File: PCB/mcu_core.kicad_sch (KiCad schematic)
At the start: 10 parts

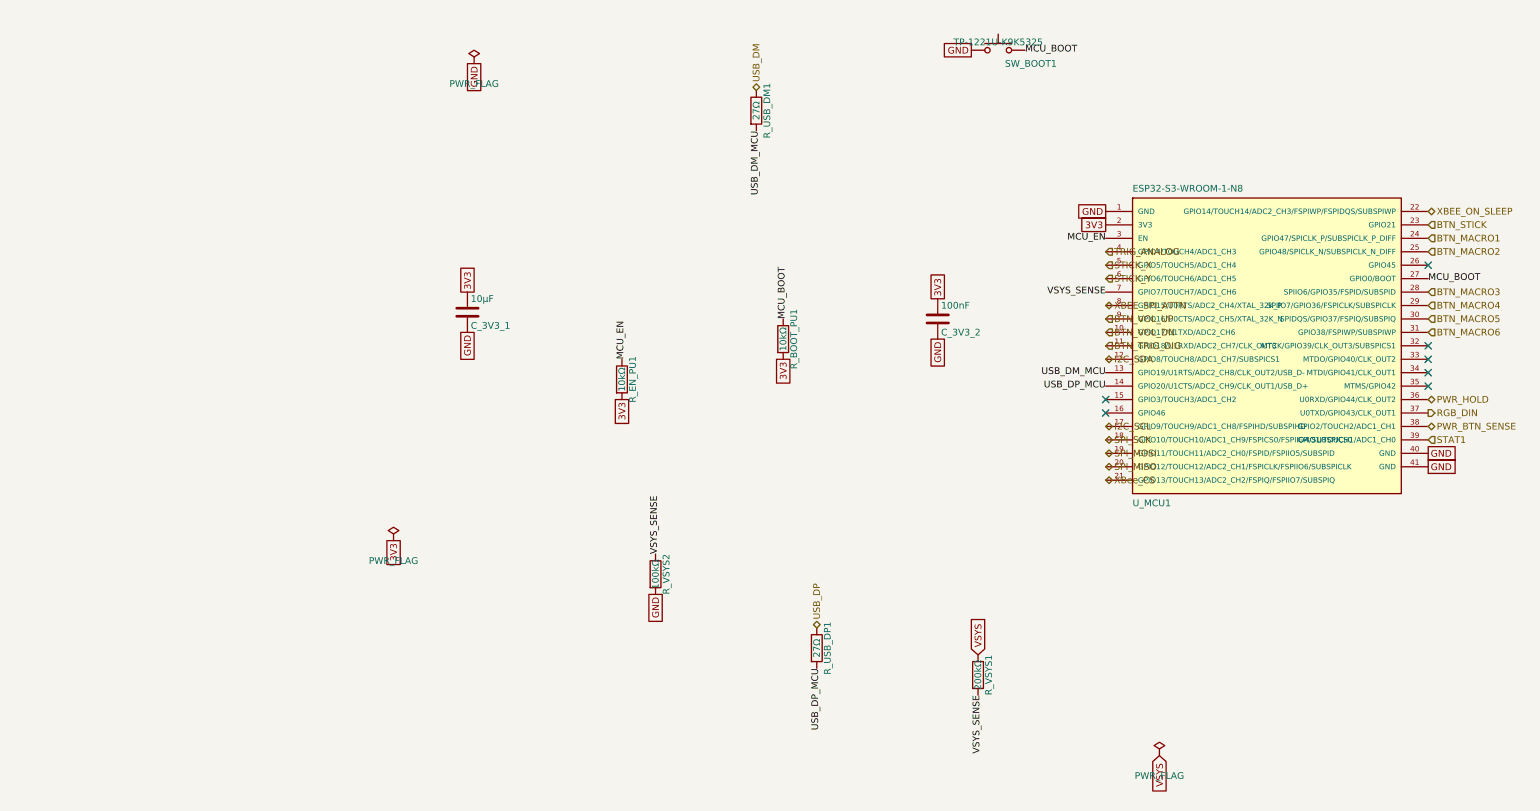
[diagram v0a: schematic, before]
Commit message: refactor: updated gulikit footprint
This updates the gulikit thumbstick footprint to be accurate.
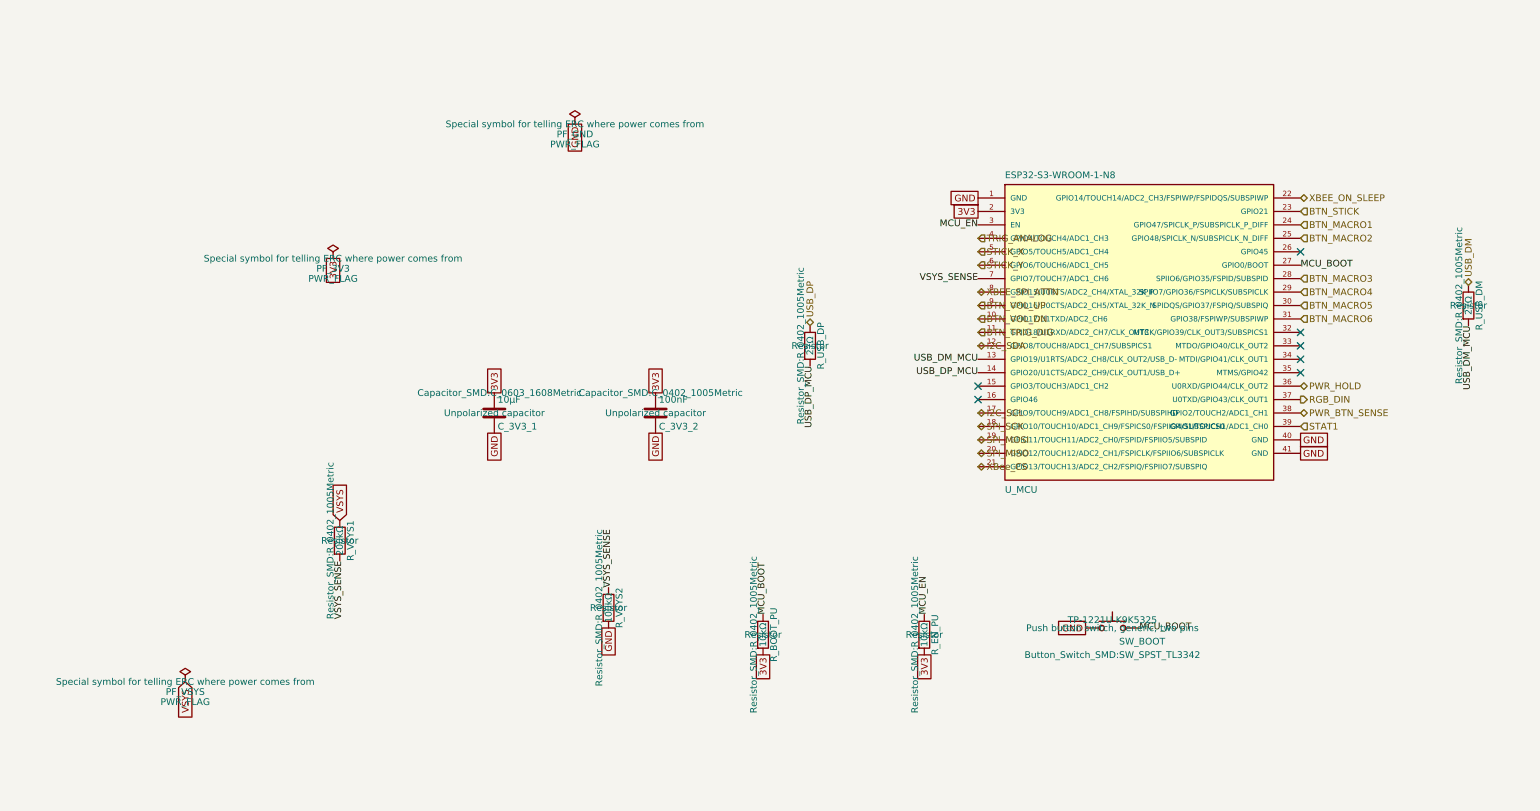
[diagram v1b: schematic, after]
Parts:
- removed R_BOOT_PU1, R_EN_PU1: 10kΩ, Resistor_SMD:R_0402_1005Metric, symbol Device:R
- removed R_USB_DM1, R_USB_DP1: 27Ω, Resistor_SMD:R_0402_1005Metric, symbol Device:R
- removed SW_BOOT1: TP-1221U-K9K5325, Button_Switch_SMD:SW_SPST_TL3342, symbol Switch:SW_Push
- removed U_MCU1: ESP32-S3-WROOM-1-N8, Espressif:ESP32-S3-WROOM-1, symbol Espressif:ESP32-S3-WROOM-1
- added PF_3V3, PF_GND, PF_VSYS: PWR_FLAG, symbol power:PWR_FLAG
- added R_BOOT_PU, R_EN_PU: 10kΩ, Resistor_SMD:R_0402_1005Metric, symbol Device:R
- added R_USB_DM, R_USB_DP: 27Ω, Resistor_SMD:R_0402_1005Metric, symbol Device:R
- added SW_BOOT: TP-1221U-K9K5325, Button_Switch_SMD:SW_SPST_TL3342, symbol Switch:SW_Push
- added U_MCU: ESP32-S3-WROOM-1-N8, Espressif:ESP32-S3-WROOM-1, symbol Espressif:ESP32-S3-WROOM-1
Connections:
- net 3V3: now also PF_3V3.1, R_BOOT_PU.2, R_EN_PU.2, U_MCU.2 (3V3)
- net BTN_MACRO1: now also U_MCU.24 (GPIO47/SPICLK_P/SUBSPICLK_P_DIFF)
- net BTN_MACRO2: now also U_MCU.25 (GPIO48/SPICLK_N/SUBSPICLK_N_DIFF)
- net BTN_MACRO3: now also U_MCU.28 (SPIIO6/GPIO35/FSPID/SUBSPID)
- net BTN_MACRO4: now also U_MCU.29 (SPIIO7/GPIO36/FSPICLK/SUBSPICLK)
- net BTN_MACRO5: now also U_MCU.30 (SPIDQS/GPIO37/FSPIQ/SUBSPIQ)
- net BTN_MACRO6: now also U_MCU.31 (GPIO38/FSPIWP/SUBSPIWP)
- net BTN_STICK: now also U_MCU.23 (GPIO21)
- net BTN_TRIG_DIG: now also U_MCU.11 (GPIO18/U1RXD/ADC2_CH7/CLK_OUT3)
- net BTN_VOL_DN: now also U_MCU.10 (GPIO17/U1TXD/ADC2_CH6)
- net BTN_VOL_UP: now also U_MCU.9 (GPIO16/U0CTS/ADC2_CH5/XTAL_32K_N)
- net GND: now also PF_GND.1, SW_BOOT.1, U_MCU.1 (GND), U_MCU.40 (GND), U_MCU.41 (GND)
- net I2C_SCL: now also U_MCU.17 (GPIO9/TOUCH9/ADC1_CH8/FSPIHD/SUBSPIHD)
- net I2C_SDA: now also U_MCU.12 (GPIO8/TOUCH8/ADC1_CH7/SUBSPICS1)
- net MCU_BOOT: now also R_BOOT_PU.1, SW_BOOT.2, U_MCU.27 (GPIO0/BOOT)
- net MCU_EN: now also R_EN_PU.1, U_MCU.3 (EN)
- net PWR_BTN_SENSE: now also U_MCU.38 (GPIO2/TOUCH2/ADC1_CH1)
- net PWR_HOLD: now also U_MCU.36 (U0RXD/GPIO44/CLK_OUT2)
- net RGB_DIN: now also U_MCU.37 (U0TXD/GPIO43/CLK_OUT1)
- net SPI_MISO: now also U_MCU.20 (GPIO12/TOUCH12/ADC2_CH1/FSPICLK/FSPIIO6/SUBSPICLK)
- net SPI_MOSI: now also U_MCU.19 (GPIO11/TOUCH11/ADC2_CH0/FSPID/FSPIIO5/SUBSPID)
- net SPI_SCK: now also U_MCU.18 (GPIO10/TOUCH10/ADC1_CH9/FSPICS0/FSPIIO4/SUBSPICS0)
- net STAT1: now also U_MCU.39 (GPIO1/TOUCH1/ADC1_CH0)
- net STICK_X: now also U_MCU.5 (GPIO5/TOUCH5/ADC1_CH4)
- net STICK_Y: now also U_MCU.6 (GPIO6/TOUCH6/ADC1_CH5)
- net TRIG_ANALOG: now also U_MCU.4 (GPIO4/TOUCH4/ADC1_CH3)
- net USB_DM: now also R_USB_DM.1
- net USB_DM_MCU: now also R_USB_DM.2, U_MCU.13 (GPIO19/U1RTS/ADC2_CH8/CLK_OUT2/USB_D-)
- net USB_DP: now also R_USB_DP.1
- net USB_DP_MCU: now also R_USB_DP.2, U_MCU.14 (GPIO20/U1CTS/ADC2_CH9/CLK_OUT1/USB_D+)
- net VSYS: now also PF_VSYS.1
- net VSYS_SENSE: now also U_MCU.7 (GPIO7/TOUCH7/ADC1_CH6)
- net XBEE_ON_SLEEP: now also U_MCU.22 (GPIO14/TOUCH14/ADC2_CH3/FSPIWP/FSPIDQS/SUBSPIWP)
- net XBEE_SPI_ATTN: now also U_MCU.8 (GPIO15/U0RTS/ADC2_CH4/XTAL_32K_P)
- net XBee_CS: now also U_MCU.21 (GPIO13/TOUCH13/ADC2_CH2/FSPIQ/FSPIIO7/SUBSPIQ)

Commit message: layout: beginning pcb layout
This updates the schematic with a few different footprints while also starts the layout.
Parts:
- removed PF_3V3, PF_GND, PF_VSYS: PWR_FLAG, symbol power:PWR_FLAG
- renumbered R_BOOT_PU to R_BOOT_PU1, R_EN_PU to R_EN_PU1, R_USB_DM to R_USB_DM1, R_USB_DP to R_USB_DP1, SW_BOOT to SW_BOOT1, U_MCU to U_MCU1
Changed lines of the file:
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@@
 		(dnp no)
 		(fields_autoplaced yes)
-		(property "Reference" "PF_GND"
+		(property "Reference" "PF_GND01"
 			(at 100.33 53.975 0)
 			(show_name no)
@@
 		)
 		(instances
+			(project "snips_controller"
+				(path "/868f8289-8434-4465-b2f4-2accc5e40bab/c3894f85-0389-4f3d-bfa3-88715bea0c3d"
+					(reference "PF_GND01")
+					(unit 1)
+				)
+			)
 			(project ""
 				(path "/d0f5b7d7-b2b6-4492-958c-e60265d3c6b4/c3894f85-0389-4f3d-bfa3-88715bea0c3d"
@@
 		(dnp no)
 		(fields_autoplaced yes)
-		(property "Reference" "U_MCU"
+		(property "Reference" "U_MCU1"
 			(at 181.61 121.92 0)
 			(show_name no)
@@
 		)
 		(instances
+			(project "snips_controller"
+				(path "/868f8289-8434-4465-b2f4-2accc5e40bab/c3894f85-0389-4f3d-bfa3-88715bea0c3d"
+					(reference "U_MCU1")
+					(unit 1)
+				)
+			)
 			(project ""
 				(path "/d0f5b7d7-b2b6-4492-958c-e60265d3c6b4/c3894f85-0389-4f3d-bfa3-88715bea0c3d"
@@
 		(dnp no)
 		(fields_autoplaced yes)
-		(property "Reference" "R_USB_DM"
+		(property "Reference" "R_USB_DM1"
 			(at 271.272 86.36 90)
 			(show_name no)
@@
 		)
 		(instances
+			(project "snips_controller"
+				(path "/868f8289-8434-4465-b2f4-2accc5e40bab/c3894f85-0389-4f3d-bfa3-88715bea0c3d"
+					(reference "R_USB_DM1")
+					(unit 1)
+				)
+			)
 			(project ""
 				(path "/d0f5b7d7-b2b6-4492-958c-e60265d3c6b4/c3894f85-0389-4f3d-bfa3-88715bea0c3d"
@@
 		(dnp no)
 		(fields_autoplaced yes)
-		(property "Reference" "R_EN_PU"
+		(property "Reference" "R_EN_PU1"
 			(at 168.402 148.59 90)
 			(show_name no)
@@
 		)
 		(instances
+			(project "snips_controller"
+				(path "/868f8289-8434-4465-b2f4-2accc5e40bab/c3894f85-0389-4f3d-bfa3-88715bea0c3d"
+					(reference "R_EN_PU1")
+					(unit 1)
+				)
+			)
 			(project ""
 				(path "/d0f5b7d7-b2b6-4492-958c-e60265d3c6b4/c3894f85-0389-4f3d-bfa3-88715bea0c3d"
@@
 		(dnp no)
 		(fields_autoplaced yes)
-		(property "Reference" "PF_VSYS"
+		(property "Reference" "PF_VSYS01"
 			(at 26.67 159.385 0)
 			(show_name no)
@@
 		)
 		(instances
+			(project "snips_controller"
+				(path "/868f8289-8434-4465-b2f4-2accc5e40bab/c3894f85-0389-4f3d-bfa3-88715bea0c3d"
+					(reference "PF_VSYS01")
+					(unit 1)
+				)
+			)
 			(project ""
 				(path "/d0f5b7d7-b2b6-4492-958c-e60265d3c6b4/c3894f85-0389-4f3d-bfa3-88715bea0c3d"
@@
 		(dnp no)
 		(fields_autoplaced yes)
-		(property "Reference" "R_BOOT_PU"
+		(property "Reference" "R_BOOT_PU1"
 			(at 137.922 148.59 90)
 			(show_name no)
@@
 		)
 		(instances
+			(project "snips_controller"
+				(path "/868f8289-8434-4465-b2f4-2accc5e40bab/c3894f85-0389-4f3d-bfa3-88715bea0c3d"
+					(reference "R_BOOT_PU1")
+					(unit 1)
+				)
+			)
 			(project ""
 				(path "/d0f5b7d7-b2b6-4492-958c-e60265d3c6b4/c3894f85-0389-4f3d-bfa3-88715bea0c3d"
@@
 		)
 		(instances
+			(project "snips_controller"
+				(path "/868f8289-8434-4465-b2f4-2accc5e40bab/c3894f85-0389-4f3d-bfa3-88715bea0c3d"
+					(reference "PF_3V3")
+					(unit 1)
+				)
+			)
 			(project ""
 				(path "/d0f5b7d7-b2b6-4492-958c-e60265d3c6b4/c3894f85-0389-4f3d-bfa3-88715bea0c3d"
@@
 		)
 		(instances
+			(project "snips_controller"
+				(path "/868f8289-8434-4465-b2f4-2accc5e40bab/c3894f85-0389-4f3d-bfa3-88715bea0c3d"
+					(reference "R_VSYS1")
+					(unit 1)
+				)
+			)
 			(project ""
 				(path "/d0f5b7d7-b2b6-4492-958c-e60265d3c6b4/c3894f85-0389-4f3d-bfa3-88715bea0c3d"
@@
 		)
 		(instances
+			(project "snips_controller"
+				(path "/868f8289-8434-4465-b2f4-2accc5e40bab/c3894f85-0389-4f3d-bfa3-88715bea0c3d"
+					(reference "C_3V3_2")
+					(unit 1)
+				)
+			)
 			(project ""
 				(path "/d0f5b7d7-b2b6-4492-958c-e60265d3c6b4/c3894f85-0389-4f3d-bfa3-88715bea0c3d"
@@
 		(dnp no)
 		(fields_autoplaced yes)
-		(property "Reference" "SW_BOOT"
+		(property "Reference" "SW_BOOT1"
 			(at 203.2 149.86 0)
 			(show_name no)
@@
 		)
 		(instances
+			(project "snips_controller"
+				(path "/868f8289-8434-4465-b2f4-2accc5e40bab/c3894f85-0389-4f3d-bfa3-88715bea0c3d"
+					(reference "SW_BOOT1")
+					(unit 1)
+				)
+			)
 			(project ""
 				(path "/d0f5b7d7-b2b6-4492-958c-e60265d3c6b4/c3894f85-0389-4f3d-bfa3-88715bea0c3d"
@@
 		)
 		(instances
+			(project "snips_controller"
+				(path "/868f8289-8434-4465-b2f4-2accc5e40bab/c3894f85-0389-4f3d-bfa3-88715bea0c3d"
+					(reference "C_3V3_1")
+					(unit 1)
+				)
+			)
 			(project ""
 				(path "/d0f5b7d7-b2b6-4492-958c-e60265d3c6b4/c3894f85-0389-4f3d-bfa3-88715bea0c3d"
@@
 		)
 		(instances
+			(project "snips_controller"
+				(path "/868f8289-8434-4465-b2f4-2accc5e40bab/c3894f85-0389-4f3d-bfa3-88715bea0c3d"
+					(reference "R_VSYS2")
+					(unit 1)
+				)
+			)
 			(project ""
 				(path "/d0f5b7d7-b2b6-4492-958c-e60265d3c6b4/c3894f85-0389-4f3d-bfa3-88715bea0c3d"
@@
 		(dnp no)
 		(fields_autoplaced yes)
-		(property "Reference" "R_USB_DP"
+		(property "Reference" "R_USB_DP1"
 			(at 146.812 93.98 90)
 			(show_name no)
@@
 		)
 		(instances
-			(project ""
-				(path "/d0f5b7d7-b2b6-4492-958c-e60265d3c6b4/c3894f85-0389-4f3d-bfa3-88715bea0c3d"
+			(project "snips_controller"
+				(path "/868f8289-8434-4465-b2f4-2accc5e40bab/c3894f85-0389-4f3d-bfa3-88715bea0c3d"
+					(reference "R_USB_DP1")
+					(unit 1)
+				)
+			)
+			(project ""
+				(path "/d0f5b7d7-b2b6-4492-958c-e60265d3c6b4/c3894f85-0389-4f3d-bfa3-88715bea0c3d"

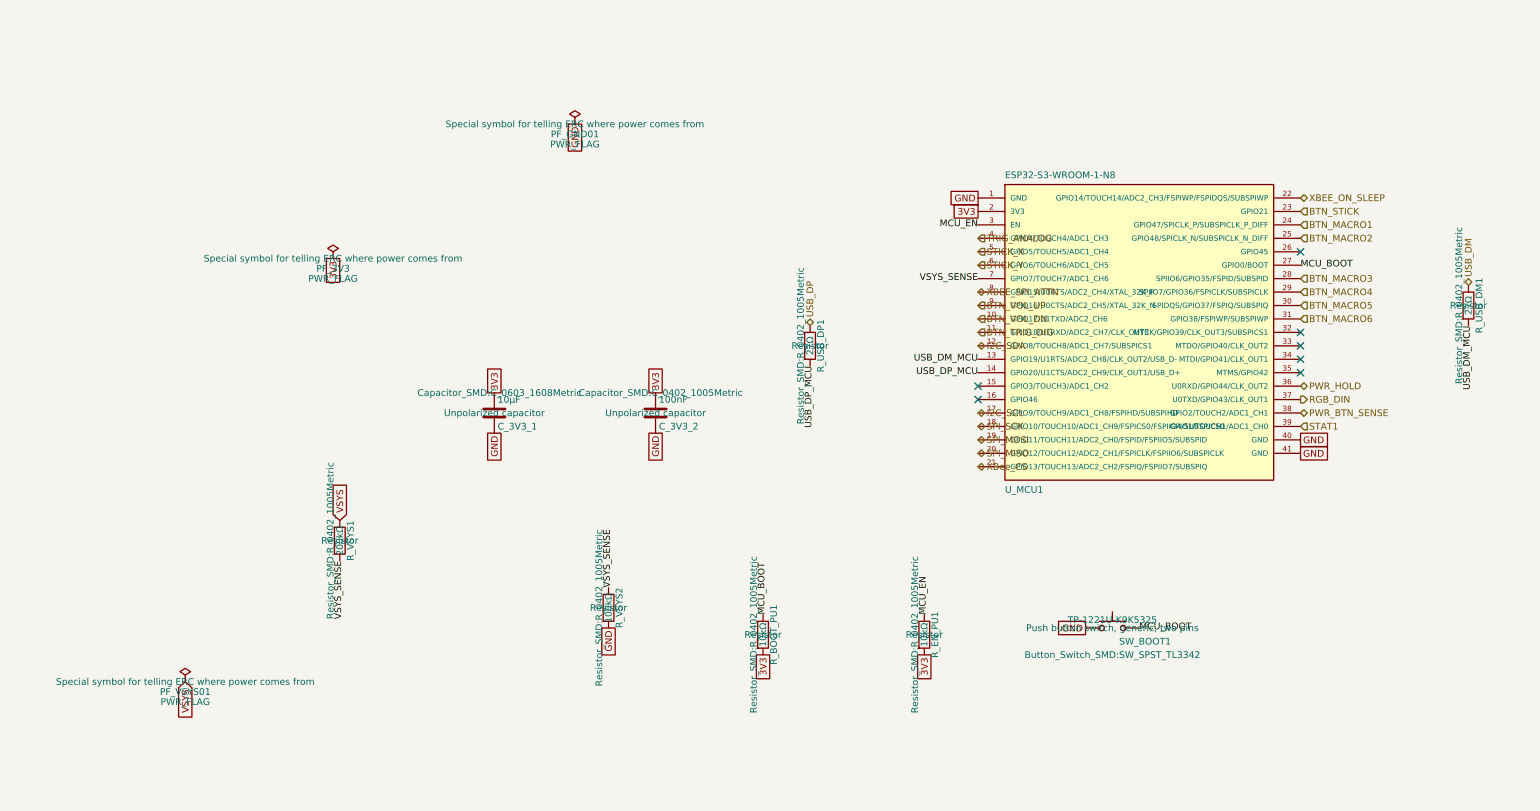
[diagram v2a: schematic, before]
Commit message: refactor: swap footprints and add symmetry
This updates the footprints of a couple components to be smaller and closer to what we want. It also adds two buttons to ensure left and right side symmetry.
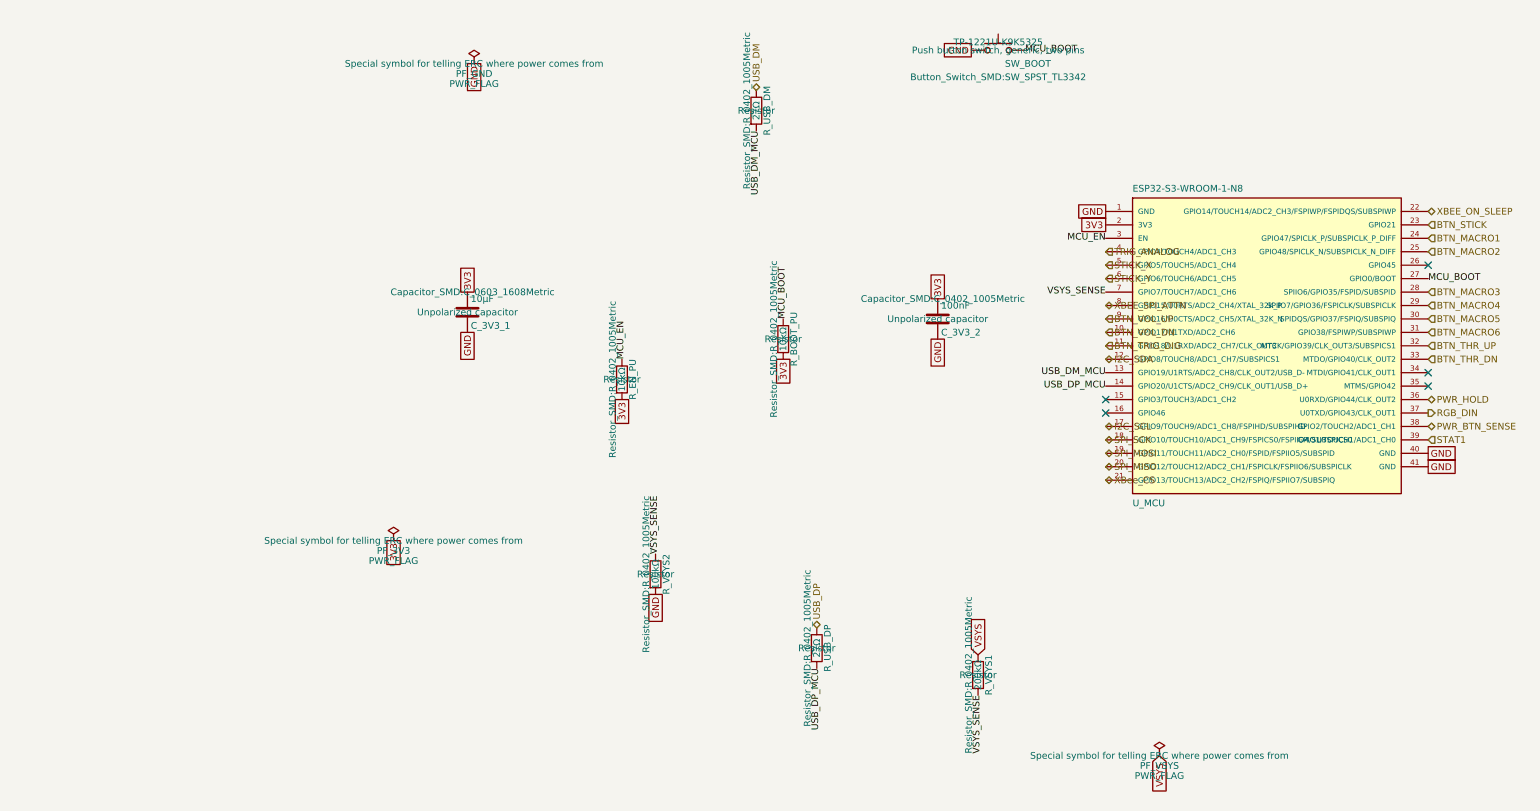
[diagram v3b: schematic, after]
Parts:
- removed R_BOOT_PU1, R_EN_PU1: 10kΩ, Resistor_SMD:R_0402_1005Metric, symbol Device:R
- removed R_USB_DM1, R_USB_DP1: 27Ω, Resistor_SMD:R_0402_1005Metric, symbol Device:R
- removed SW_BOOT1: TP-1221U-K9K5325, Button_Switch_SMD:SW_SPST_TL3342, symbol Switch:SW_Push
- removed U_MCU1: ESP32-S3-WROOM-1-N8, Espressif:ESP32-S3-WROOM-1, symbol Espressif:ESP32-S3-WROOM-1
- added PF_3V3, PF_GND, PF_VSYS: PWR_FLAG, symbol power:PWR_FLAG
- added R_BOOT_PU, R_EN_PU: 10kΩ, Resistor_SMD:R_0402_1005Metric, symbol Device:R
- added R_USB_DM, R_USB_DP: 27Ω, Resistor_SMD:R_0402_1005Metric, symbol Device:R
- added SW_BOOT: TP-1221U-K9K5325, Button_Switch_SMD:SW_SPST_TL3342, symbol Switch:SW_Push
- added U_MCU: ESP32-S3-WROOM-1-N8, Espressif:ESP32-S3-WROOM-1, symbol Espressif:ESP32-S3-WROOM-1
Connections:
- net 3V3: now also PF_3V3.1, R_BOOT_PU.2, R_EN_PU.2, U_MCU.2 (3V3)
- net BTN_MACRO1: now also U_MCU.24 (GPIO47/SPICLK_P/SUBSPICLK_P_DIFF)
- net BTN_MACRO2: now also U_MCU.25 (GPIO48/SPICLK_N/SUBSPICLK_N_DIFF)
- net BTN_MACRO3: now also U_MCU.28 (SPIIO6/GPIO35/FSPID/SUBSPID)
- net BTN_MACRO4: now also U_MCU.29 (SPIIO7/GPIO36/FSPICLK/SUBSPICLK)
- net BTN_MACRO5: now also U_MCU.30 (SPIDQS/GPIO37/FSPIQ/SUBSPIQ)
- net BTN_MACRO6: now also U_MCU.31 (GPIO38/FSPIWP/SUBSPIWP)
- net BTN_STICK: now also U_MCU.23 (GPIO21)
- net BTN_TRIG_DIG: now also U_MCU.11 (GPIO18/U1RXD/ADC2_CH7/CLK_OUT3)
- net BTN_VOL_DN: now also U_MCU.10 (GPIO17/U1TXD/ADC2_CH6)
- net BTN_VOL_UP: now also U_MCU.9 (GPIO16/U0CTS/ADC2_CH5/XTAL_32K_N)
- net GND: now also PF_GND.1, SW_BOOT.1, U_MCU.1 (GND), U_MCU.40 (GND), U_MCU.41 (GND)
- net I2C_SCL: now also U_MCU.17 (GPIO9/TOUCH9/ADC1_CH8/FSPIHD/SUBSPIHD)
- net I2C_SDA: now also U_MCU.12 (GPIO8/TOUCH8/ADC1_CH7/SUBSPICS1)
- net MCU_BOOT: now also R_BOOT_PU.1, SW_BOOT.2, U_MCU.27 (GPIO0/BOOT)
- net MCU_EN: now also R_EN_PU.1, U_MCU.3 (EN)
- net PWR_BTN_SENSE: now also U_MCU.38 (GPIO2/TOUCH2/ADC1_CH1)
- net PWR_HOLD: now also U_MCU.36 (U0RXD/GPIO44/CLK_OUT2)
- net RGB_DIN: now also U_MCU.37 (U0TXD/GPIO43/CLK_OUT1)
- net SPI_MISO: now also U_MCU.20 (GPIO12/TOUCH12/ADC2_CH1/FSPICLK/FSPIIO6/SUBSPICLK)
- net SPI_MOSI: now also U_MCU.19 (GPIO11/TOUCH11/ADC2_CH0/FSPID/FSPIIO5/SUBSPID)
- net SPI_SCK: now also U_MCU.18 (GPIO10/TOUCH10/ADC1_CH9/FSPICS0/FSPIIO4/SUBSPICS0)
- net STAT1: now also U_MCU.39 (GPIO1/TOUCH1/ADC1_CH0)
- net STICK_X: now also U_MCU.5 (GPIO5/TOUCH5/ADC1_CH4)
- net STICK_Y: now also U_MCU.6 (GPIO6/TOUCH6/ADC1_CH5)
- net TRIG_ANALOG: now also U_MCU.4 (GPIO4/TOUCH4/ADC1_CH3)
- net USB_DM: now also R_USB_DM.1
- net USB_DM_MCU: now also R_USB_DM.2, U_MCU.13 (GPIO19/U1RTS/ADC2_CH8/CLK_OUT2/USB_D-)
- net USB_DP: now also R_USB_DP.1
- net USB_DP_MCU: now also R_USB_DP.2, U_MCU.14 (GPIO20/U1CTS/ADC2_CH9/CLK_OUT1/USB_D+)
- net VSYS: now also PF_VSYS.1
- net VSYS_SENSE: now also U_MCU.7 (GPIO7/TOUCH7/ADC1_CH6)
- net XBEE_ON_SLEEP: now also U_MCU.22 (GPIO14/TOUCH14/ADC2_CH3/FSPIWP/FSPIDQS/SUBSPIWP)
- net XBEE_SPI_ATTN: now also U_MCU.8 (GPIO15/U0RTS/ADC2_CH4/XTAL_32K_P)
- net XBee_CS: now also U_MCU.21 (GPIO13/TOUCH13/ADC2_CH2/FSPIQ/FSPIIO7/SUBSPIQ)
- new net BTN_THR_DN: U_MCU.33 (MTDO/GPIO40/CLK_OUT2)
- new net BTN_THR_UP: U_MCU.32 (MTCK/GPIO39/CLK_OUT3/SUBSPICS1)
- no-connect marks 7 -> 5
